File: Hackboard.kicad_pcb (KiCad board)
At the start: 2 copper layers, 61 parts, among them J1 Conn_01x31_Socket, J2 Micro_SD_Card, J3 Conn_01x31_Socket, J5 Barrel_Jack, J6 USB_C_Receptacle_USB2.0_16P, J7 Conn_02x02_Counter_Clockwise, Q1 NMOS, Q2 NMOS, Q3 NMOS, SW1 SW_MEC_5E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

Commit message: Make basis of out line and start placing components
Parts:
- added A1: Arduino_UNO_R3_WithMountingHoles, Module:Arduino_UNO_R3_WithMountingHoles, F.Cu at (31.2, -4.32)
- added H1: MountingHole, MountingHole:MountingHole_3.2mm_M3, F.Cu at (144.0, 96.0)
- added H2: MountingHole, MountingHole:MountingHole_3.2mm_M3, F.Cu at (144.0, 68.1)
- added H3: MountingHole, MountingHole:MountingHole_3.2mm_M3, F.Cu at (91.9, 63.0)
- added H4: MountingHole, MountingHole:MountingHole_3.2mm_M3, F.Cu at (93.2, 111.3)
- D5: value D_Schottky -> LED; footprint DO-221AC:VSSAF3L63HM3 -> LED_SMD:LED_0603_1608Metric
- D6: value LED -> D_Schottky; footprint LED_SMD:LED_0603_1608Metric -> DO-221AC:VSSAF3L63HM3
- J5: value Barrel_Jack -> Conn_02x02_Counter_Clockwise; footprint Connector_BarrelJack:CUI_PJ-002AH -> Connector_PinHeader_2.54mm:PinHeader_2x02_P2.54mm_Vertical
- J7: value Conn_02x02_Counter_Clockwise -> Barrel_Jack_Switch; footprint Connector_PinHeader_2.54mm:PinHeader_2x02_P2.54mm_Vertical -> Connector_BarrelJack:CUI_PJ-002AH
- R11: value 5k1 -> 10k
- R13: value 10k -> 5k1
- R15: value 220R -> 10k
- R7: value 10k -> 220R
- R8: value 200R -> 10k
- R9: value 10k -> 200R
- SW1: value SW_MEC_5E -> SW_DPST
- moved J2 208.1 mm to (182.1, 88.1), turned to 90 degrees
- moved U6 188.6 mm to (150.9, 105.2), turned to 90 degrees
- moved U4 183.4 mm to (137.2, 69.5), turned to -90 degrees
- moved U3 182.7 mm to (141.7, 85.1), turned to 180 degrees
- moved U5 181.5 mm to (134.1, 105.2), turned to 90 degrees
- moved J1 181.4 mm to (109.5, 111.3), turned to 90 degrees
- moved U9 174.5 mm to (164.6, 69.8), turned to -90 degrees
- moved J3 158.9 mm to (105.9, 63.0), turned to 90 degrees
- moved U8 142.2 mm to (122.4, 69.8), turned to -90 degrees
- moved J7 117.1 mm to (85.3, 98.6), turned to 180 degrees
- moved J6 110.2 mm to (81.5, 68.1), turned to -90 degrees
- moved SW1 98.2 mm to (81.8, 83.1), turned to 90 degrees
- moved J5 20.0 mm to (-28.1, 81.5)
- moved D5 14.5 mm to (-37.9, 95.3)
- moved D6 14.3 mm to (-27.1, 100.3)
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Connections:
- D1 pad 2: LED_PIN31 -> +3V3
- D2 pad 2: LED_PIN32 -> LED_PIN31
- D3 pad 2: LED_PIN33 -> LED_PIN32
- D4 pad 2: LED_PIN34 -> LED_PIN33
- D5 pad 1: +5V -> Net-(D5-K)
- D5 pad 2: Net-(D5-A) -> LED_PIN34
- D6 pad 1: Net-(D6-K) -> +5V
- D6 pad 2: +3V3 -> Net-(D6-A)
- J5 pad 1: VCC -> SW_SWCLK
- J5 pad 2: GND -> SW_SWDIO
- J5 pad 3: (no net) -> GND
- J6 pad A4: Net-(D5-A) -> Net-(D6-A)
- J7 pad 1: SW_SWCLK -> VCC
- J7 pad 2: SW_SWDIO -> GND
- R10 pad 1: +3V3 -> I2C_SCL_A5
- R10 pad 2: I2C_SDA_A4 -> +3V3
- R11 pad 1: Net-(J6-CC1) -> +3V3
- R11 pad 2: +3V3 -> I2C_SDA_A4
- R12 pad 1: Net-(J6-CC2) -> Net-(J6-CC1)
- R13 pad 1: SCL -> Net-(J6-CC2)
- R13 pad 2: +5V -> +3V3
- R14 pad 1: +5V -> SCL
- R14 pad 2: SDA -> +5V
- R15 pad 1: Net-(D6-K) -> +5V
- R15 pad 2: GND -> SDA
- R3 pad 2: Net-(JP1-B) -> GND
- R7 pad 1: PWM_PIN2 -> Net-(D5-K)
- R7 pad 2: GND -> Net-(JP1-B)
- R8 pad 1: Net-(Q1-G) -> PWM_PIN2
- R8 pad 2: PWM_PIN2 -> GND
- R9 pad 1: I2C_SCL_A5 -> Net-(Q1-G)
- R9 pad 2: +3V3 -> PWM_PIN2
- SW1 pad 2: GND -> RESET
- U5 pad 10: PWM_PIN15_O -> UART_RX_PIN8_O
- U5 pad 12: PWM_PIN15 -> UART_RX_PIN8
- U5 pad 13: PWM_PIN14 -> UART_TX_PIN9
- U5 pad 14: PWM_PIN13 -> PWM_PIN10
- U5 pad 15: USB_DN_PIN12 -> USB_DP_PIN11
- U5 pad 16: USB_DP_PIN11 -> USB_DN_PIN12
- U5 pad 17: PWM_PIN10 -> PWM_PIN13
- U5 pad 18: UART_TX_PIN9 -> PWM_PIN14
- U5 pad 19: UART_RX_PIN8 -> PWM_PIN15
- U5 pad 3: UART_RX_PIN8_O -> PWM_PIN15_O
- U5 pad 4: UART_TX_PIN9_O -> PWM_PIN14_O
- U5 pad 5: PWM_PIN10_O -> PWM_PIN13_O
- U5 pad 6: USB_DP_PIN11_O -> USB_DN_PIN12_O
- U5 pad 7: USB_DN_PIN12_O -> USB_DP_PIN11_O
- U5 pad 8: PWM_PIN13_O -> PWM_PIN10_O
- U5 pad 9: PWM_PIN14_O -> UART_TX_PIN9_O
- U6 pad 10: GPIO_PIN7_O -> CAN_TX_PIN0_O
- U6 pad 12: GPIO_PIN7 -> CAN_TX_PIN0
- U6 pad 13: GPIO_PIN6 -> CAN_RX_PIN1
- U6 pad 14: PWM_PIN5 -> Net-(JP2-B)
- U6 pad 15: SD_MOSI_GPIO_PIN4 -> PWM_PIN3
- U6 pad 16: PWM_PIN3 -> SD_MOSI_GPIO_PIN4
- U6 pad 17: Net-(JP2-B) -> PWM_PIN5
- U6 pad 18: CAN_RX_PIN1 -> GPIO_PIN6
- U6 pad 19: CAN_TX_PIN0 -> GPIO_PIN7
- U6 pad 3: CAN_TX_PIN0_O -> GPIO_PIN7_O
- U6 pad 4: CAN_RX_PIN1_O -> GPIO_PIN6_O
- U6 pad 5: PWM_PIN2_O -> PWM_PIN5_O
- U6 pad 6: PWM_PIN3_O -> GPIO_PIN4_O
- U6 pad 7: GPIO_PIN4_O -> PWM_PIN3_O
- U6 pad 8: PWM_PIN5_O -> PWM_PIN2_O
- U6 pad 9: GPIO_PIN6_O -> CAN_RX_PIN1_O
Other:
- board outline added: 110.5 x 53.8 mm
- board text removed: "Copyright (C) 2024 Adam Turaj This program is free software: you can redistribute it and/or modify it under the terms of the GNU General Public License as published by the Free Software Foundation, either version 3 of the License, or (at your option) any later version. This program is distributed in the hope that it will be useful, but WITHOUT ANY WARRANTY; without even the implied warranty of ME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"

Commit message: Continue Laying down parts
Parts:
- removed A1: Arduino_UNO_R3_WithMountingHoles, Module:Arduino_UNO_R3_WithMountingHoles
- added C17: 0.1uF, Capacitor_SMD:C_0603_1608Metric, F.Cu at (136.1, 94.2)
- moved R9 207.7 mm to (167.4, 100.8), turned to 90 degrees
- moved Q1 207.3 mm to (164.8, 100.8), turned to 90 degrees
- moved R8 206.8 mm to (166.6, 97.8), turned to 180 degrees
- moved JP2 196.7 mm to (168.4, 95.5)
- moved C5 183.6 mm to (133.4, 97.5), turned to 180 degrees
- moved C6 182.5 mm to (133.3, 96.0), turned to 180 degrees
- moved C14 181.3 mm to (137.9, 86.1), turned to 180 degrees
- moved C15 180.4 mm to (137.9, 84.6), turned to 180 degrees
- moved C16 179.1 mm to (137.9, 80.0), turned to 180 degrees
- moved FB1 178.3 mm to (137.2, 82.3), turned to 90 degrees
- moved C8 177.3 mm to (132.3, 80.8)
- moved R1 174.7 mm to (131.1, 96.8), turned to -90 degrees
- moved C4 171.8 mm to (125.2, 79.2)
- moved C10 170.1 mm to (125.2, 80.8)
- moved C13 167.9 mm to (121.7, 92.7), turned to 90 degrees
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
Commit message: Start routing PCB
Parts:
- moved R15 52.3 mm to (103.9, 73.4), turned to 90 degrees
- moved R14 44.8 mm to (96.5, 73.4), turned to -90 degrees
- moved R11 43.0 mm to (98.8, 73.4), turned to -90 degrees
- moved R12 39.3 mm to (87.9, 66.5)
- moved R13 37.2 mm to (87.8, 72.1)
- moved R10 34.6 mm to (90.9, 73.7), turned to 90 degrees
- moved C16 23.0 mm to (127.8, 100.6), turned to -90 degrees
- moved C15 22.9 mm to (123.2, 102.1), turned to 90 degrees
- moved C14 22.8 mm to (121.6, 102.1), turned to 90 degrees
- moved FB1 22.4 mm to (125.5, 101.3), turned to 0 degrees
- moved C8 17.2 mm to (124.5, 96.0), turned to 180 degrees
- moved C5 14.7 mm to (145.8, 89.7), turned to 0 degrees
- moved C6 12.5 mm to (136.9, 84.1), turned to -90 degrees
- moved C17 12.1 mm to (124.5, 97.5), turned to 180 degrees
- moved R1 12.1 mm to (120.9, 90.2), turned to 180 degrees
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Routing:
- net +3V3: track 0.00 -> 131.7 mm, vias 0 -> 2
- net PWM_PIN13_O: track 0.00 -> 50.9 mm
- net PWM_PIN14_O: track 0.00 -> 50.1 mm
- net PWM_PIN15_O: track 0.00 -> 49.3 mm
- net +5V: track 0.00 -> 34.9 mm
- net I2C_SCL_A5: track 0.00 -> 30.4 mm, vias 0 -> 1
- net ANALOG_A7: track 0.00 -> 28.9 mm, vias 0 -> 1
- net SD_SCK_DAC_A8: track 0.00 -> 28.1 mm
- net I2C_SDA_A4: track 0.00 -> 27.6 mm, vias 0 -> 1
- net ANALOG_A6: track 0.00 -> 26.5 mm, vias 0 -> 1
- net DAC_A0: track 0.00 -> 25.0 mm, vias 0 -> 1
- net OPAMP_OUT_A3: track 0.00 -> 20.3 mm
- net OPAMP_N_A2: track 0.00 -> 18.3 mm
- net OPAMP_P_A1: track 0.00 -> 17.5 mm
- net Net-(JP1-B): track 0.00 -> 15.6 mm
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- added copper zone on F.Cu, net GND

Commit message: Continue tracing
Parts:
- moved C15 15.1 mm to (136.9, 95.8)
- moved FB1 15.1 mm to (139.2, 95.0)
- moved C16 14.5 mm to (141.5, 95.8), turned to 90 degrees
- moved J5 14.4 mm to (117.9, 82.3)
- moved C14 11.2 mm to (131.6, 97.0)
- moved C5 9.31 mm to (136.9, 92.5), turned to -90 degrees
- moved D4 4.91 mm to (110.5, 80.4)
- moved R6 4.91 mm to (110.5, 83.7)
- moved D2 4.91 mm to (114.0, 80.4)
- moved D3 4.91 mm to (112.3, 80.4)
- moved D5 4.91 mm to (108.7, 80.4)
- moved JP1 4.91 mm to (111.5, 88.5)
- moved R4 4.91 mm to (114.0, 83.7)
- moved R5 4.91 mm to (112.3, 83.7)
- moved R7 4.91 mm to (108.7, 83.7)
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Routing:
- net USB_DP_PIN11: track 0.00 -> 84.9 mm, vias 0 -> 4
- net USB_DN_PIN12: track 0.00 -> 84.2 mm, vias 0 -> 4
- net +3V3: track 131.7 -> 52.2 mm, vias 2 -> 0
- net GPIO_PIN6: track 0.00 -> 61.7 mm, vias 0 -> 2
- net GPIO_PIN7: track 0.00 -> 60.9 mm, vias 0 -> 2
- net UART_TX_PIN9: track 0.00 -> 48.8 mm, vias 0 -> 2
- net UART_RX_PIN8: track 0.00 -> 47.7 mm, vias 0 -> 2
- net PWM_PIN10: track 0.00 -> 47.4 mm, vias 0 -> 2
- net SPI_CS_PIN35: track 0.00 -> 42.3 mm, vias 0 -> 2
- net LED_PIN33: track 3.89 -> 44.7 mm, vias 0 -> 2
- net LED_PIN31: track 0.00 -> 39.1 mm, vias 0 -> 3
- net PWM_PIN14: track 0.00 -> 38.9 mm, vias 0 -> 2
- net PWM_PIN13: track 0.00 -> 38.0 mm, vias 0 -> 2
- net PWM_PIN16: track 0.00 -> 37.4 mm, vias 0 -> 2
- net LED_PIN34: track 3.67 -> 40.6 mm, vias 0 -> 2
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- added copper zone on B.Cu, net GND

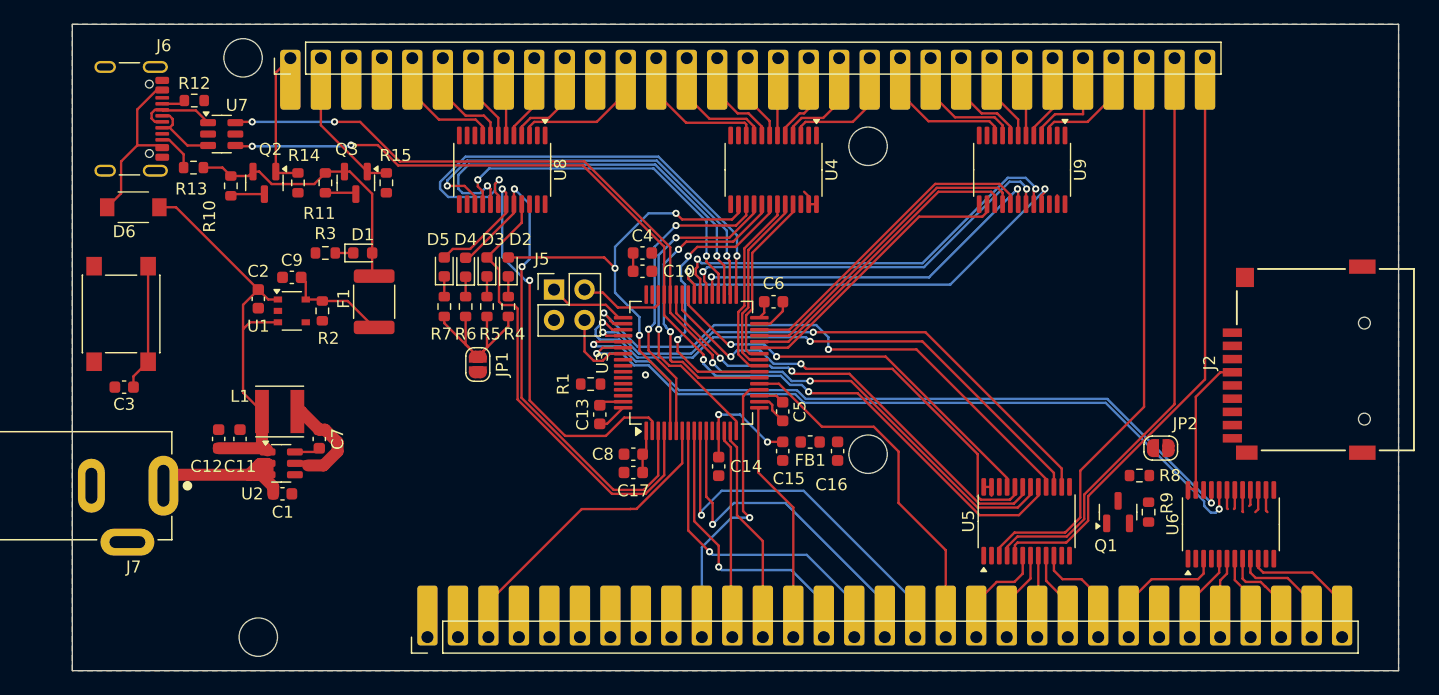
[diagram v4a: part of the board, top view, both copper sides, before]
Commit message: Finish tracing MCU pins
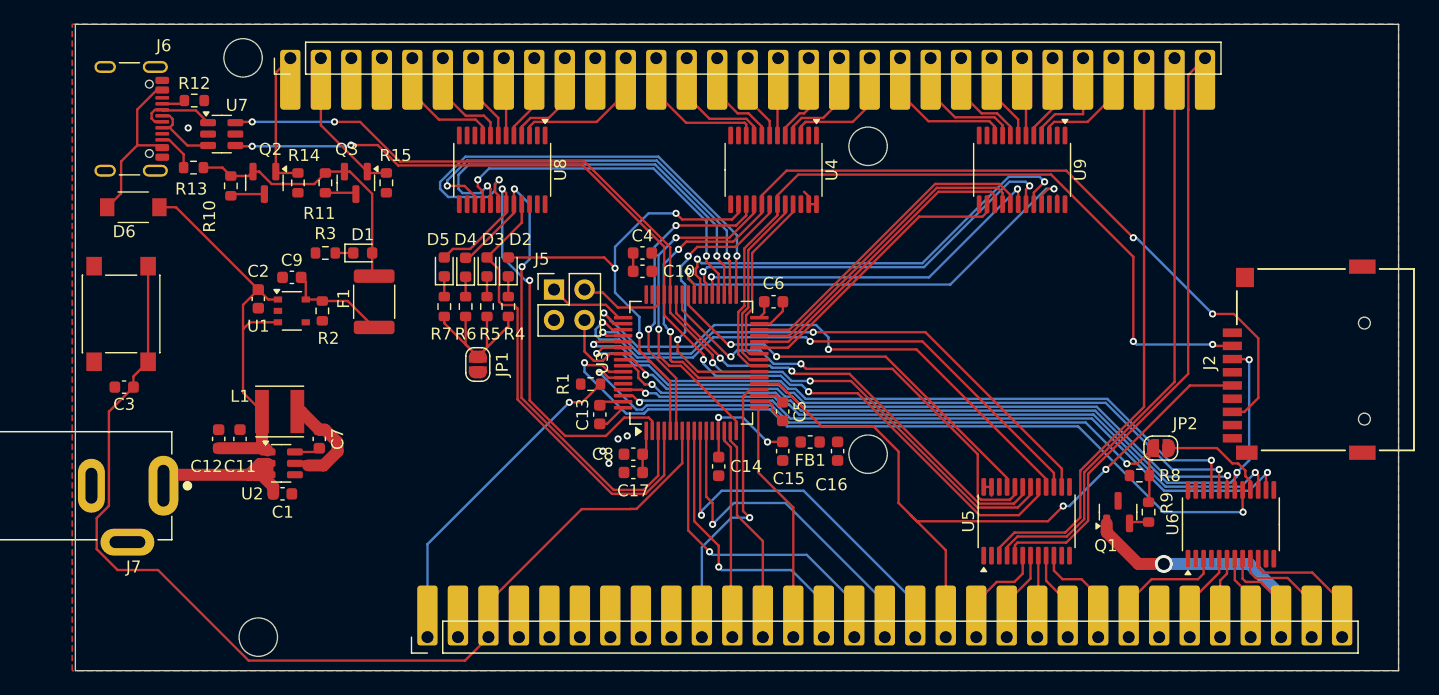
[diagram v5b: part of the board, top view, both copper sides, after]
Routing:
- net SD_MOSI_GPIO_PIN4: track 1.62 -> 68.8 mm, vias 0 -> 3
- net PWM_PIN3: track 1.86 -> 66.1 mm, vias 0 -> 2
- net CAN_TX_PIN0: track 1.90 -> 59.3 mm, vias 0 -> 2
- net PWM_PIN2: track 0.00 -> 56.9 mm, vias 0 -> 2
- net SD_MISO_PWM_28: track 26.9 -> 83.3 mm, vias 2 -> 4
- net CAN_RX_PIN1: track 1.95 -> 58.1 mm, vias 0 -> 2
- net PWM_PIN5: track 1.62 -> 55.8 mm, vias 1 -> 2
- net RESET: track 37.1 -> 89.2 mm
- net SD_CS_PWM_26: track 16.0 -> 65.4 mm, vias 0 -> 2
- net SD_SCK_DAC_A8: track 31.0 -> 62.7 mm, vias 0 -> 2
- net BOOT: track 0.00 -> 27.7 mm, vias 0 -> 1
- net PWM_PIN2_O: track 8.09 -> 29.0 mm, vias 0 -> 1
- net +3V3: track 52.2 -> 40.5 mm
- net Net-(JP2-B): track 1.38 -> 8.96 mm
- net GPIO_PIN6: track 61.7 -> 60.0 mm
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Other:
- board size 110.5 x 53.8 mm -> 110.2 x 53.8 mm

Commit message: Route power
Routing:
- net GND: track 8.11 -> 143.2 mm, vias 5 -> 40
- net I2C_SCL_A5: track 30.4 -> 85.3 mm, vias 1 -> 3
- net I2C_SDA_A4: track 27.6 -> 82.4 mm, vias 1 -> 3
- net +3V3: track 40.5 -> 52.0 mm, vias 0 -> 17
- net VDDA: track 9.52 -> 11.0 mm
- net SD_MOSI_GPIO_PIN4: track 68.8 -> 69.7 mm
- net ANALOG_A7: track 32.7 -> 32.1 mm
- added copper zone on F.Cu, net +3V3
- added copper zone on In2.Cu, net +3V3
- added copper zone on In1.Cu, net GND
- removed copper zone on B.Cu, net GND
- removed copper zone on F.Cu, net GND
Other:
- copper layers 2 -> 4

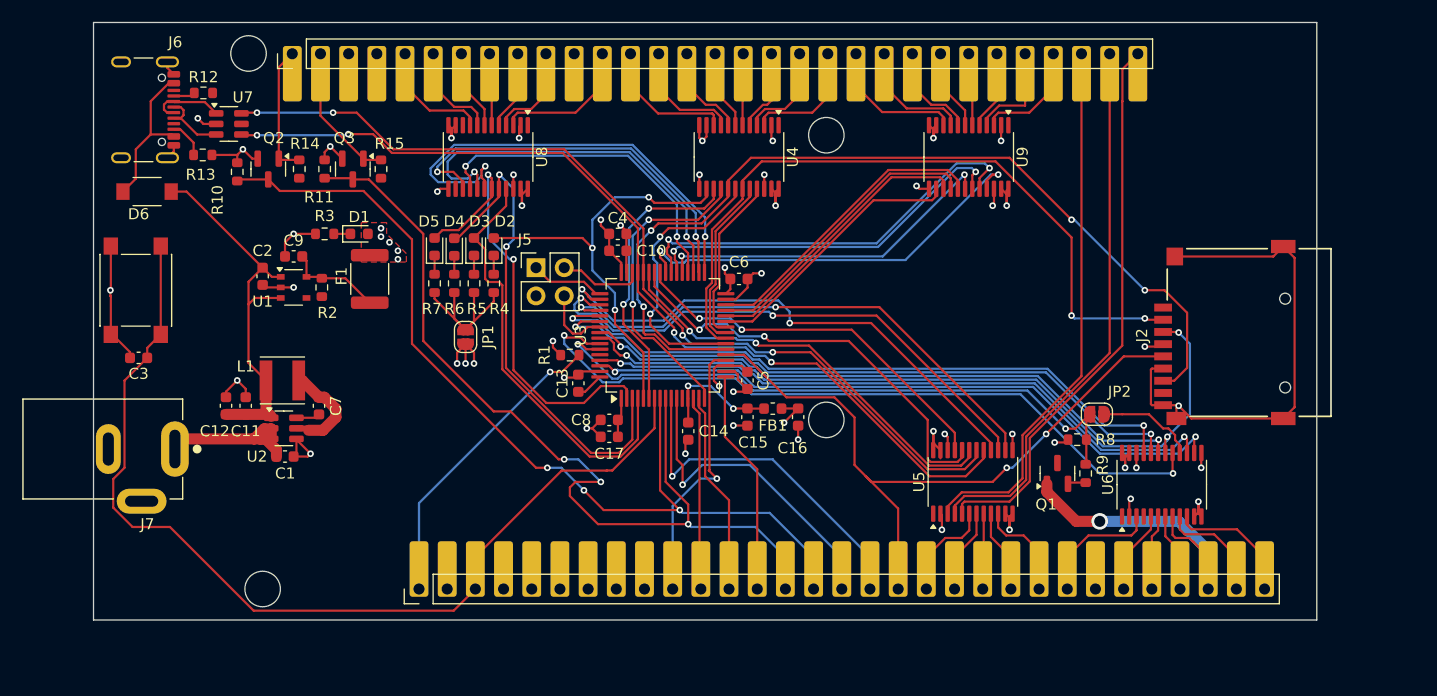
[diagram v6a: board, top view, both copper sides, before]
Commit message: Change USB C footprint, fix DRC errors, adjust silkscreen
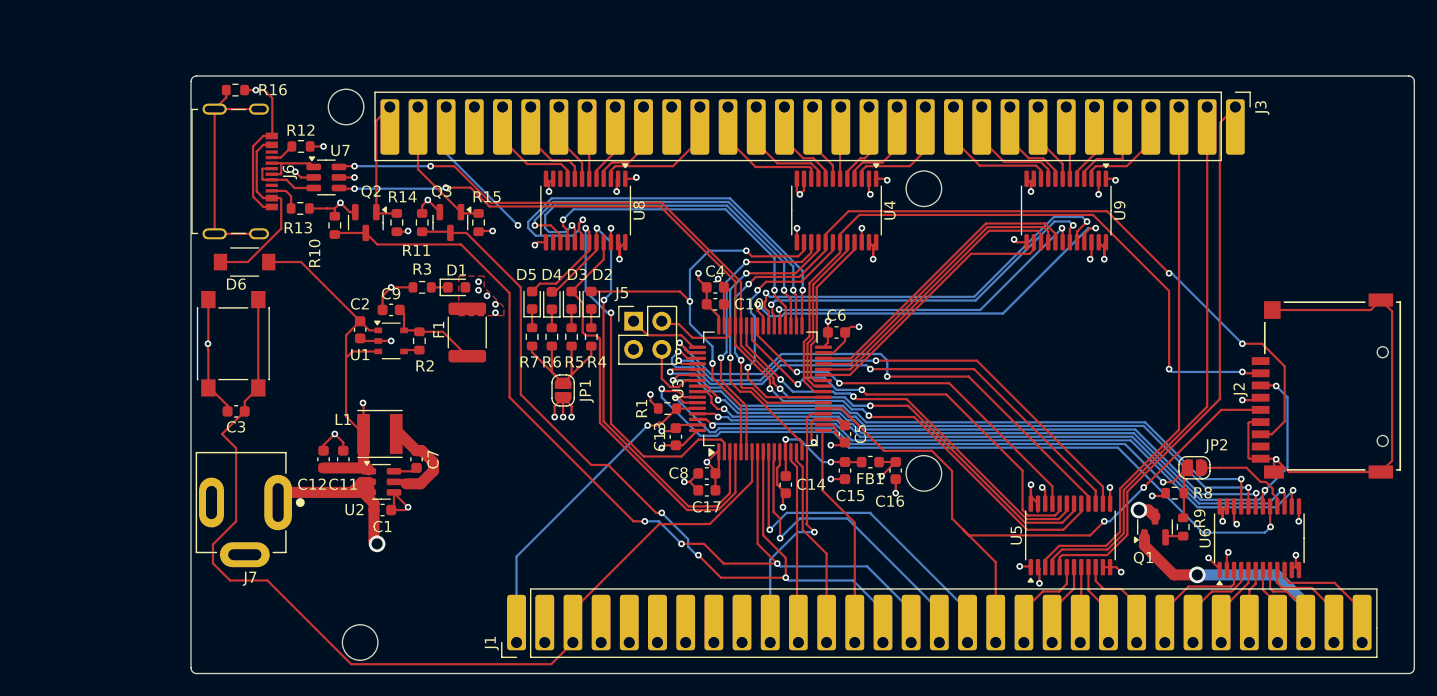
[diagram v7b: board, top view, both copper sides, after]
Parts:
- added R16: 1M, Resistor_SMD:R_0603_1608Metric, F.Cu at (90.8, 66.3)
- J6: footprint Connector_USB:USB_C_Receptacle_GCT_USB4105-xx-A_16P_TopMnt_Horizontal -> Connector_USB:USB_C_Receptacle_Molex_216990
- moved J3 85.1 mm to (180.9, 67.8), turned to -90 degrees
- moved D6 10.8 mm to (91.6, 81.8)
- moved J7 10.5 mm to (94.6, 103.5)
- moved C1 10.0 mm to (104.0, 104.1)
- moved C13 10.0 mm to (130.5, 97.5)
- moved D4 10.0 mm to (119.3, 85.3)
- moved R6 10.0 mm to (119.3, 88.5)
- moved R9 10.0 mm to (176.2, 105.7)
- moved U3 10.0 mm to (138.1, 93.2)
- moved U5 10.0 mm to (166.0, 106.4)
- moved U6 10.0 mm to (183.0, 106.7)
- moved H3 10.0 mm to (100.7, 67.8)
- moved C14 10.0 mm to (140.4, 101.9)
- moved H1 10.0 mm to (152.8, 100.8)
- moved H2 10.0 mm to (152.8, 75.2)
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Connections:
- J6 pad S1: GND -> Net-(J6-SHIELD)
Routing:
- net +5V: track 34.9 -> 240.9 mm, vias 0 -> 9
- net VCC: track 14.4 -> 101.6 mm, vias 0 -> 2
- net VDDA: track 11.0 -> 61.1 mm, vias 2 -> 3
- net Net-(J6-SHIELD): track 0.00 -> 21.4 mm
- net GND: track 143.2 -> 158.5 mm, vias 40 -> 41
- net GPIO_PIN6_O: track 0.00 -> 9.37 mm
- net I2C_SDA_A4: track 82.4 -> 76.8 mm
- net +3V3: track 52.0 -> 57.4 mm, vias 17 -> 20
- net Net-(D6-A): track 14.5 -> 17.1 mm
- net BOOT: track 27.7 -> 29.6 mm
- net Net-(U1-PG): track 0.00 -> 1.43 mm
- net Net-(J6-D--PadA7): track 6.71 -> 5.72 mm
- net RESET: track 89.2 -> 90.1 mm
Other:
- outline, holes or cut-outs redrawn
